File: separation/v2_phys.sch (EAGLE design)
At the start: 8 parts

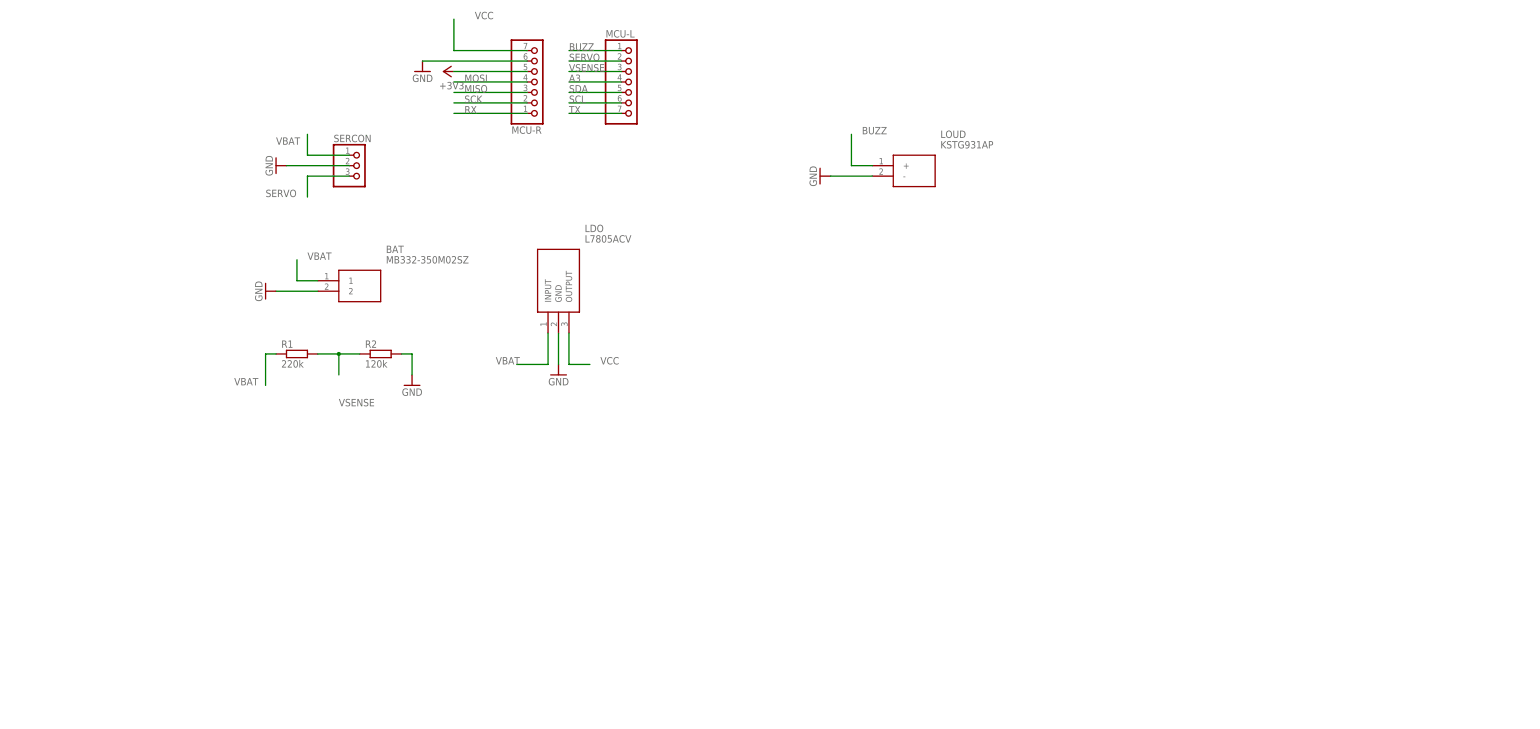
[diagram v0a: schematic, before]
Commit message: add 3x pressure sensors to physical model
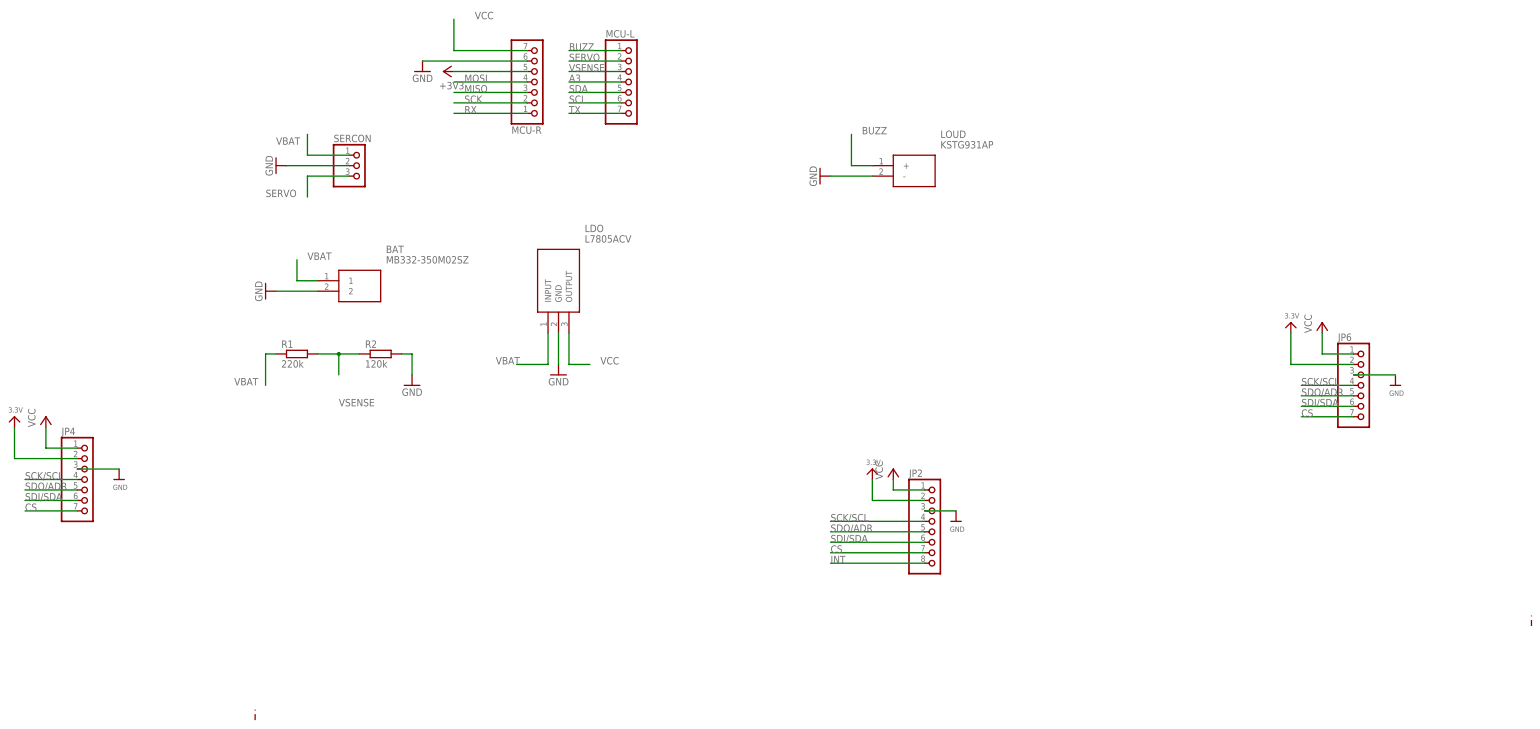
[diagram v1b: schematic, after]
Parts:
- added JP2: (no value), microbuilder:HEADER-1X870MIL
- added JP4, JP6: (no value), microbuilder:HEADER-1X770MIL
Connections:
- new net 3.3V: JP2.2, JP4.2, JP6.2
- new net CS: JP2.7, JP4.7, JP6.7
- new net INT: JP2.8
- new net SCK/SCL: JP2.4, JP4.4, JP6.4
- new net SDI/SDA: JP2.6, JP4.6, JP6.6
- new net SDO/ADR: JP2.5, JP4.5, JP6.5
- net GND: now also JP2.3, JP4.3, JP6.3
- net VCC: now also JP2.1, JP4.1, JP6.1
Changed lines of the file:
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@@
 <class number="0" name="default" width="0" drill="0">
 </class>
-<class number="1" name="power" width="0.3048" drill="0">
+<class number="1" name="highpower" width="0.3048" drill="0.4826">
+</class>
+<class number="2" name="lowpower" width="0.3048" drill="0.4826">
 </class>
 </classes>
@@
 <part name="R2" library="rcl" library_urn="urn:adsk.eagle:library:334" deviceset="R-EU_" device="0204/2V" package3d_urn="urn:adsk.eagle:package:23495/1" value="120k"/>
 <part name="GND6" library="supply1" library_urn="urn:adsk.eagle:library:371" deviceset="GND" device=""/>
+<part name="U$1" library="microbuilder" deviceset="GND" device=""/>
+<part name="U$2" library="microbuilder" deviceset="3.3V" device=""/>
+<part name="JP2" library="microbuilder" deviceset="HEADER-1X8" device="70MIL"/>
+<part name="P+1" library="supply1" library_urn="urn:adsk.eagle:library:371" deviceset="VCC" device=""/>
+<part name="U$5" library="microbuilder" deviceset="GND" device=""/>
+<part name="U$6" library="microbuilder" deviceset="3.3V" device=""/>
+<part name="P+2" library="supply1" library_urn="urn:adsk.eagle:library:371" deviceset="VCC" device=""/>
+<part name="JP4" library="microbuilder" deviceset="HEADER-1X7" device="70MIL"/>
+<part name="U$9" library="microbuilder" deviceset="GND" device=""/>
+<part name="U$11" library="microbuilder" deviceset="3.3V" device=""/>
+<part name="P+6" library="supply1" library_urn="urn:adsk.eagle:library:371" deviceset="VCC" device=""/>
+<part name="JP6" library="microbuilder" deviceset="HEADER-1X7" device="70MIL"/>
 </parts>
 <sheets>
 <sheet>
 <plain>
+<wire x1="-30.48" y1="-96.52" x2="-30.48" y2="-93.98" width="0.1524" layer="94" style="shortdash"/>
+<wire x1="279.4" y1="-73.66" x2="279.4" y2="-71.12" width="0.1524" layer="94" style="shortdash"/>
 </plain>
 <instances>
@@
 <attribute name="VALUE" x="10.16" y="-17.78" size="1.778" layer="96" rot="MR0"/>
 </instance>
+<instance part="U$1" gate="G$1" x="139.7" y="-48.26" smashed="yes">
+<attribute name="VALUE" x="138.176" y="-50.8" size="1.27" layer="96"/>
+</instance>
+<instance part="U$2" gate="G$1" x="119.38" y="-35.56" smashed="yes">
+<attribute name="VALUE" x="117.856" y="-34.544" size="1.27" layer="96"/>
+</instance>
+<instance part="JP2" gate="A" x="134.62" y="-50.8" smashed="yes">
+<attribute name="NAME" x="128.27" y="-37.465" size="1.778" layer="95"/>
+<attribute name="VALUE" x="128.27" y="-63.5" size="1.778" layer="96"/>
+</instance>
+<instance part="P+1" gate="VCC" x="124.46" y="-35.56" smashed="yes">
+<attribute name="VALUE" x="121.92" y="-38.1" size="1.778" layer="96" rot="R90"/>
+</instance>
+<instance part="U$5" gate="G$1" x="-63.5" y="-38.1" smashed="yes">
+<attribute name="VALUE" x="-65.024" y="-40.64" size="1.27" layer="96"/>
+</instance>
+<instance part="U$6" gate="G$1" x="-88.9" y="-22.86" smashed="yes">
+<attribute name="VALUE" x="-90.424" y="-21.844" size="1.27" layer="96"/>
+</instance>
+<instance part="P+2" gate="VCC" x="-81.28" y="-22.86" smashed="yes">
+<attribute name="VALUE" x="-83.82" y="-25.4" size="1.778" layer="96" rot="R90"/>
+</instance>
+<instance part="JP4" gate="A" x="-71.12" y="-38.1" smashed="yes">
+<attribute name="NAME" x="-77.47" y="-27.305" size="1.778" layer="95"/>
+<attribute name="VALUE" x="-77.47" y="-50.8" size="1.778" layer="96"/>
+</instance>
+<instance part="U$9" gate="G$1" x="246.38" y="-15.24" smashed="yes">
+<attribute name="VALUE" x="244.856" y="-17.78" size="1.27" layer="96"/>
+</instance>
+<instance part="U$11" gate="G$1" x="220.98" y="0" smashed="yes">
+<attribute name="VALUE" x="219.456" y="1.016" size="1.27" layer="96"/>
+</instance>
+<instance part="P+6" gate="VCC" x="228.6" y="0" smashed="yes">
+<attribute name="VALUE" x="226.06" y="-2.54" size="1.778" layer="96" rot="R90"/>
+</instance>
+<instance part="JP6" gate="A" x="238.76" y="-15.24" smashed="yes">
+<attribute name="NAME" x="232.41" y="-4.445" size="1.778" layer="95"/>
+<attribute name="VALUE" x="232.41" y="-27.94" size="1.778" layer="96"/>
+</instance>
 </instances>
 <busses>
@@
 <wire x1="7.62" y1="-7.62" x2="7.62" y2="-12.7" width="0.1524" layer="91"/>
 </segment>
+<segment>
+<pinref part="U$1" gate="G$1" pin="GND"/>
+<wire x1="132.08" y1="-45.72" x2="139.7" y2="-45.72" width="0.1524" layer="91"/>
+<pinref part="JP2" gate="A" pin="3"/>
+</segment>
+<segment>
+<pinref part="U$5" gate="G$1" pin="GND"/>
+<wire x1="-73.66" y1="-35.56" x2="-63.5" y2="-35.56" width="0.1524" layer="91"/>
+<pinref part="JP4" gate="A" pin="3"/>
+</segment>
+<segment>
+<pinref part="U$9" gate="G$1" pin="GND"/>
+<wire x1="236.22" y1="-12.7" x2="246.38" y2="-12.7" width="0.1524" layer="91"/>
+<pinref part="JP6" gate="A" pin="3"/>
+</segment>
 </net>
 <net name="MOSI" class="0">
@@
 <wire x1="45.72" y1="-10.16" x2="50.8" y2="-10.16" width="0.1524" layer="91"/>
 <label x="53.34" y="-10.16" size="1.778" layer="95"/>
+</segment>
+<segment>
+<wire x1="132.08" y1="-40.64" x2="124.46" y2="-40.64" width="0.1524" layer="91"/>
+<wire x1="124.46" y1="-40.64" x2="124.46" y2="-38.1" width="0.1524" layer="91"/>
+<pinref part="JP2" gate="A" pin="1"/>
+<pinref part="P+1" gate="VCC" pin="VCC"/>
+</segment>
+<segment>
+<wire x1="-73.66" y1="-30.48" x2="-81.28" y2="-30.48" width="0.1524" layer="91"/>
+<wire x1="-81.28" y1="-30.48" x2="-81.28" y2="-25.4" width="0.1524" layer="91"/>
+<pinref part="P+2" gate="VCC" pin="VCC"/>
+<pinref part="JP4" gate="A" pin="1"/>
+</segment>
+<segment>
+<wire x1="236.22" y1="-7.62" x2="228.6" y2="-7.62" width="0.1524" layer="91"/>
+<wire x1="228.6" y1="-7.62" x2="228.6" y2="-2.54" width="0.1524" layer="91"/>
+<pinref part="P+6" gate="VCC" pin="VCC"/>
+<pinref part="JP6" gate="A" pin="1"/>
 </segment>
 </net>
@@
 </segment>
 </net>
+<net name="3.3V" class="0">
+<segment>
+<pinref part="U$2" gate="G$1" pin="3.3V"/>
+<wire x1="132.08" y1="-43.18" x2="119.38" y2="-43.18" width="0.1524" layer="91"/>
+<wire x1="119.38" y1="-43.18" x2="119.38" y2="-38.1" width="0.1524" layer="91"/>
+<pinref part="JP2" gate="A" pin="2"/>
+</segment>
+<segment>
+<wire x1="-73.66" y1="-33.02" x2="-88.9" y2="-33.02" width="0.1524" layer="91"/>
+<wire x1="-88.9" y1="-33.02" x2="-88.9" y2="-25.4" width="0.1524" layer="91"/>
+<pinref part="U$6" gate="G$1" pin="3.3V"/>
+<pinref part="JP4" gate="A" pin="2"/>
+</segment>
+<segment>
+<wire x1="236.22" y1="-10.16" x2="220.98" y2="-10.16" width="0.1524" layer="91"/>
+<wire x1="220.98" y1="-10.16" x2="220.98" y2="-2.54" width="0.1524" layer="91"/>
+<pinref part="U$11" gate="G$1" pin="3.3V"/>
+<pinref part="JP6" gate="A" pin="2"/>
+</segment>
+</net>
+<net name="INT" class="0">
+<segment>
+<pinref part="JP2" gate="A" pin="8"/>
+<wire x1="132.08" y1="-58.42" x2="109.22" y2="-58.42" width="0.1524" layer="91"/>
+<label x="109.22" y="-58.42" size="1.778" layer="95"/>
+</segment>
+</net>
+<net name="SDO/ADR" class="0">
+<segment>
+<wire x1="132.08" y1="-50.8" x2="109.22" y2="-50.8" width="0.1524" layer="91"/>
+<label x="109.22" y="-50.8" size="1.778" layer="95"/>
+<pinref part="JP2" gate="A" pin="5"/>
+</segment>
+<segment>
+<wire x1="-73.66" y1="-40.64" x2="-86.36" y2="-40.64" width="0.1524" layer="91"/>
+<label x="-86.36" y="-40.64" size="1.778" layer="95"/>
+<pinref part="JP4" gate="A" pin="5"/>
+</segment>
+<segment>
+<wire x1="236.22" y1="-17.78" x2="223.52" y2="-17.78" width="0.1524" layer="91"/>
+<label x="223.52" y="-17.78" size="1.778" layer="95"/>
+<pinref part="JP6" gate="A" pin="5"/>
+</segment>
+</net>
+<net name="SDI/SDA" class="0">
+<segment>
+<wire x1="132.08" y1="-53.34" x2="109.22" y2="-53.34" width="0.1524" layer="91"/>
+<label x="109.22" y="-53.34" size="1.778" layer="95"/>
+<pinref part="JP2" gate="A" pin="6"/>
+</segment>
+<segment>
+<wire x1="-73.66" y1="-43.18" x2="-86.36" y2="-43.18" width="0.1524" layer="91"/>
+<label x="-86.36" y="-43.18" size="1.778" layer="95"/>
+<pinref part="JP4" gate="A" pin="6"/>
+</segment>
+<segment>
+<wire x1="236.22" y1="-20.32" x2="223.52" y2="-20.32" width="0.1524" layer="91"/>
+<label x="223.52" y="-20.32" size="1.778" layer="95"/>
+<pinref part="JP6" gate="A" pin="6"/>
+</segment>
+</net>
+<net name="SCK/SCL" class="0">
+<segment>
+<wire x1="132.08" y1="-48.26" x2="109.22" y2="-48.26" width="0.1524" layer="91"/>
+<label x="109.22" y="-48.26" size="1.778" layer="95"/>
+<pinref part="JP2" gate="A" pin="4"/>
+</segment>
+<segment>
+<wire x1="-73.66" y1="-38.1" x2="-86.36" y2="-38.1" width="0.1524" layer="91"/>
+<label x="-86.36" y="-38.1" size="1.778" layer="95"/>
+<pinref part="JP4" gate="A" pin="4"/>
+</segment>
+<segment>
+<wire x1="236.22" y1="-15.24" x2="223.52" y2="-15.24" width="0.1524" layer="91"/>
+<label x="223.52" y="-15.24" size="1.778" layer="95"/>
+<pinref part="JP6" gate="A" pin="4"/>
+</segment>
+</net>
+<net name="CS" class="0">
+<segment>
+<wire x1="132.08" y1="-55.88" x2="109.22" y2="-55.88" width="0.1524" layer="91"/>
+<label x="109.22" y="-55.88" size="1.778" layer="95"/>
+<pinref part="JP2" gate="A" pin="7"/>
+</segment>
+<segment>
+<wire x1="-73.66" y1="-45.72" x2="-86.36" y2="-45.72" width="0.1524" layer="91"/>
+<label x="-86.36" y="-45.72" size="1.778" layer="95"/>
+<pinref part="JP4" gate="A" pin="7"/>
+</segment>
+<segment>
+<wire x1="236.22" y1="-22.86" x2="223.52" y2="-22.86" width="0.1524" layer="91"/>
+<label x="223.52" y="-22.86" size="1.778" layer="95"/>
+<pinref part="JP6" gate="A" pin="7"/>
+</segment>
+</net>

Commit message: update physical map with updated board
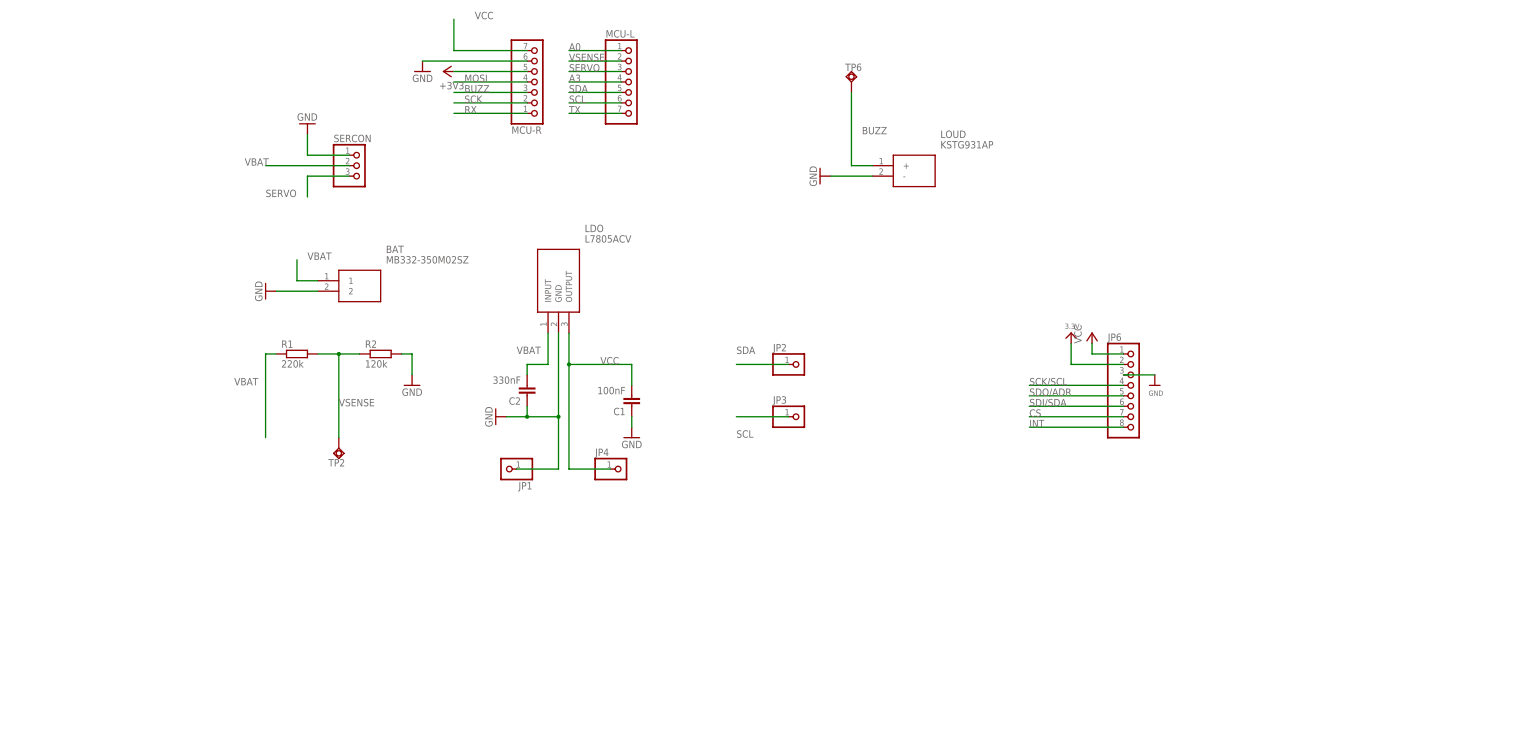
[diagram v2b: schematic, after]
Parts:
- added C1: 100nF, rcl:C-EU025-024X044
- added C2: 330nF, rcl:C-EU025-024X044
- added JP1, JP3: (no value), pinhead:PINHD-1X1
- added TP2, TP6: TPSQB2,54, testpad:TPSQB2,54
- JP2: device microbuilder:HEADER-1X870MIL -> pinhead:PINHD-1X1
- JP4: device microbuilder:HEADER-1X770MIL -> pinhead:PINHD-1X1
- JP6: device microbuilder:HEADER-1X770MIL -> microbuilder:HEADER-1X870MIL
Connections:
- removed net MISO: MCU-R.3
- new net A0: MCU-L.1
- net 3.3V: no longer JP2.2, JP4.2
- net BUZZ: now also MCU-R.3, TP6.TP; no longer MCU-L.1
- net CS: no longer JP2.7, JP4.7
- net GND: now also C1.1, C2.1, JP1.1, SERCON.1; no longer JP2.3, JP4.3, SERCON.2
- net INT: now also JP6.8; no longer JP2.8
- net SCK/SCL: no longer JP2.4, JP4.4
- net SCL: now also JP3.1
- net SDA: now also JP2.1
- net SDI/SDA: no longer JP2.6, JP4.6
- net SDO/ADR: no longer JP2.5, JP4.5
- net SERVO: now also MCU-L.3; no longer MCU-L.2
- net VBAT: now also C2.2, SERCON.2; no longer SERCON.1
- net VCC: now also C1.2; no longer JP2.1
- net VSENSE: now also MCU-L.2, TP2.TP; no longer MCU-L.3
